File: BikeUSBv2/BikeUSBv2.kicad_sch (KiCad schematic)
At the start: 51 parts, among them J1 TYPE-C-31-M-16, J2 Conn_01x02_Female, Q1 SSM3J332R,LF, Q2 SSM3J332R,LF, SW1 SW_Push, SW2 SW_Push, U1 TPS63020DSJR, U2 ATtiny1616-M

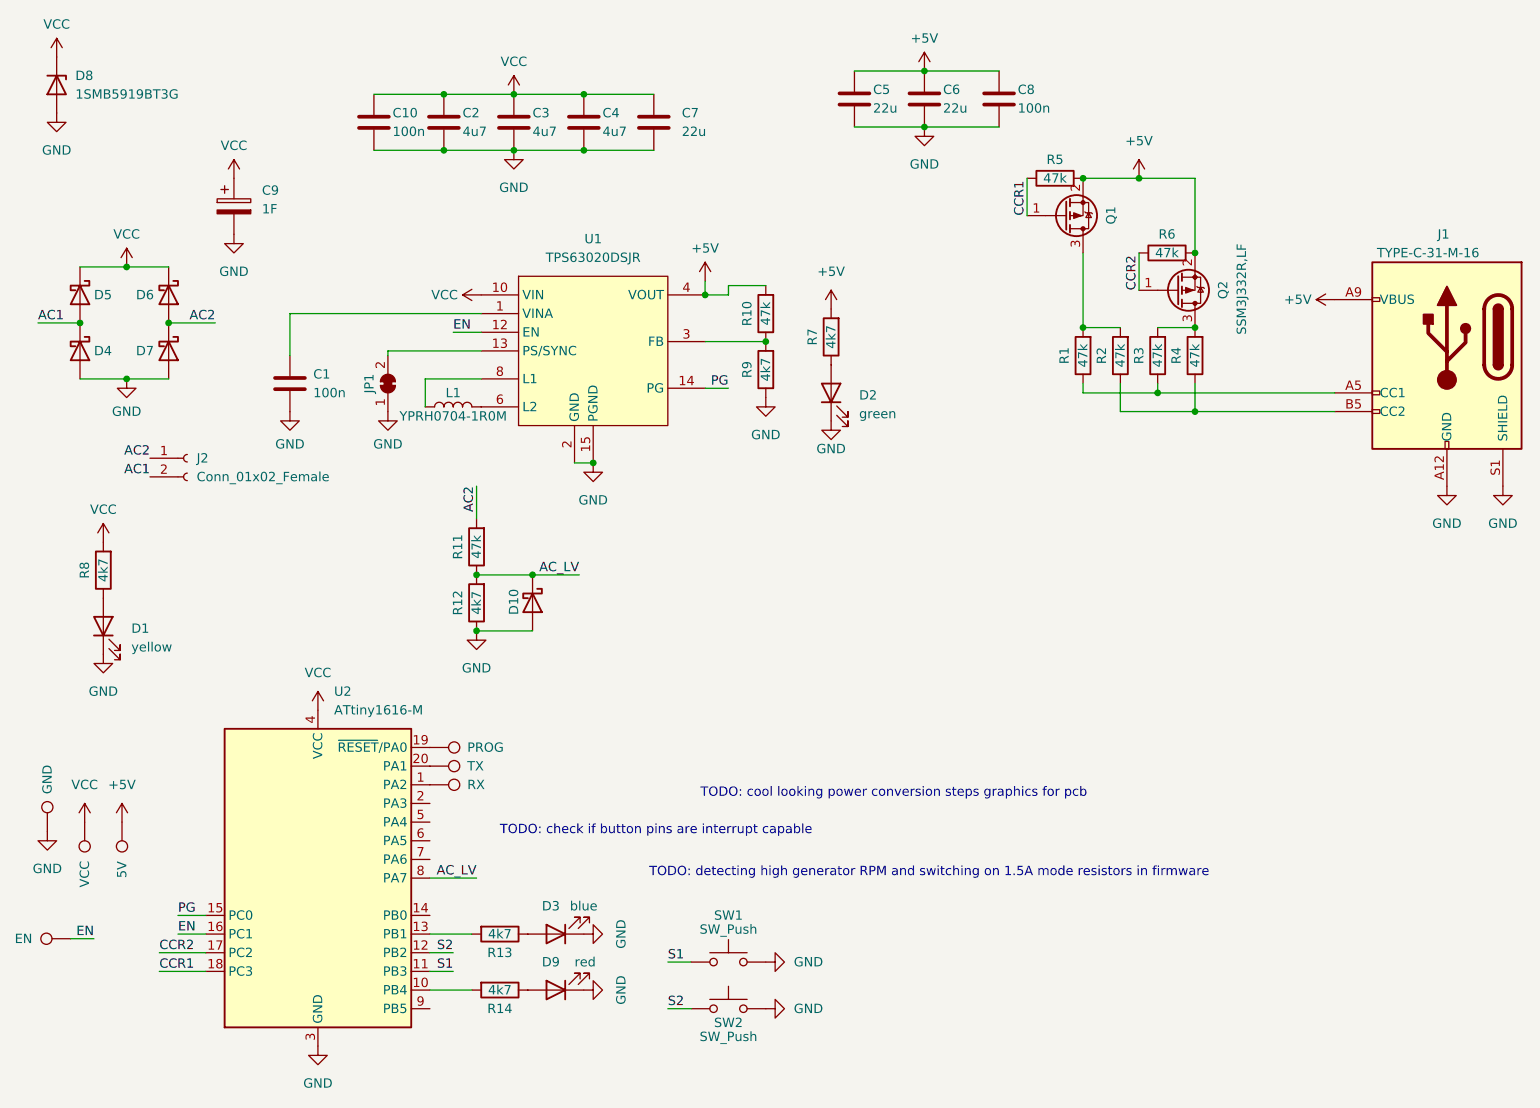
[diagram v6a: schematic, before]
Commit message: reduced component count
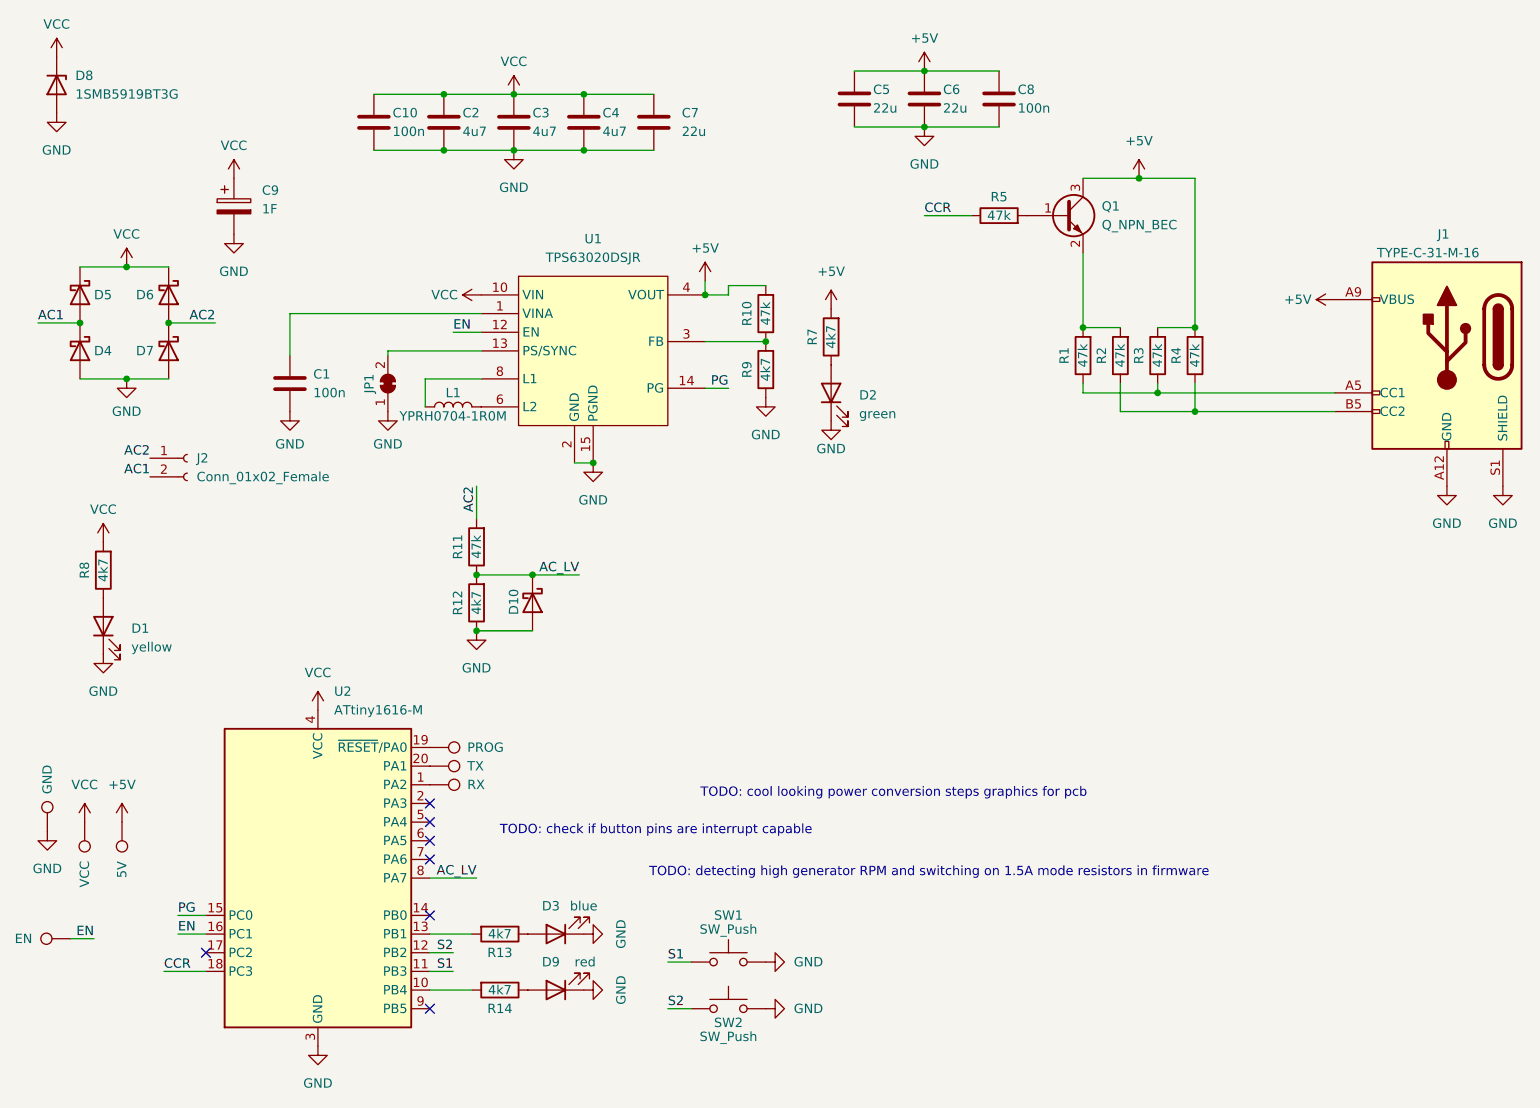
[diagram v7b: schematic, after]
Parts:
- removed Q1, Q2: SSM3J332R,LF, Package_TO_SOT_SMD:SOT-23_Handsoldering, symbol Device:Q_PMOS_GSD
- removed R6: 47k, Resistor_SMD:R_0805_2012Metric_Pad1.20x1.40mm_HandSolder, symbol Device:R
- added Q1: Q_NPN_BEC, Package_TO_SOT_SMD:SOT-23_Handsoldering, symbol Device:Q_NPN_BEC
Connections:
- net +5V: now also R3.2, R4.2, Q1.3 (C); no longer R5.2
- net at R1.2, R2.2: now also Q1.2 (E)
- net CCR1 renamed CCR
- net CCR2: no longer names the net of U2.17 (PC2)
- new net: Q1.1 (B), R5.2
- no-connect marks 0 -> 7
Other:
- moved on the sheet: R5
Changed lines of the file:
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@@
   (junction (at 85.09 122.555) (diameter 0) (color 0 0 0 0)
   )
-  (junction (at 160.02 68.58) (diameter 0) (color 0 0 0 0)
-  )
   (junction (at 29.845 80.645) (diameter 0) (color 0 0 0 0)
   )
@@
   (junction (at 92.075 64.77) (diameter 0) (color 0 0 0 0)
   )
+  (junction (at 175.26 88.9) (diameter 0) (color 0 0 0 0)
+  )
   (junction (at 93.345 107.315) (diameter 0) (color 0 0 0 0)
   )
@@
   (junction (at 138.43 53.975) (diameter 0) (color 0 0 0 0)
   )
-  (junction (at 175.26 88.9) (diameter 0) (color 0 0 0 0)
-  )
   (junction (at 77.47 122.555) (diameter 0) (color 0 0 0 0)
   )
@@
   (junction (at 167.64 68.58) (diameter 0) (color 0 0 0 0)
   )
-  (junction (at 175.26 78.74) (diameter 0) (color 0 0 0 0)
-  )
   (junction (at 175.26 100.33) (diameter 0) (color 0 0 0 0)
   )
+  (no_connect (at 71.12 153.67))
+  (no_connect (at 71.12 161.29))
+  (no_connect (at 71.12 168.91))
+  (no_connect (at 71.12 181.61))
+  (no_connect (at 71.12 156.21))
+  (no_connect (at 71.12 158.75))
+  (no_connect (at 40.64 173.99))
   (wire (pts (xy 165.1 100.33) (xy 165.1 96.52))
     (stroke (width 0) (type default))
@@
     (stroke (width 0) (type default))
   )
+  (wire (pts (xy 138.43 73.66) (xy 144.78 73.66))
+    (stroke (width 0) (type default))
+  )
   (wire (pts (xy 23.495 95.885) (xy 29.845 95.885))
     (stroke (width 0) (type default))
@@
     (stroke (width 0) (type default))
   )
-  (wire (pts (xy 167.64 78.74) (xy 167.64 83.82))
-    (stroke (width 0) (type default))
-  )
   (wire (pts (xy 170.18 97.79) (xy 170.18 96.52))
     (stroke (width 0) (type default))
@@
     (stroke (width 0) (type default))
   )
-  (wire (pts (xy 152.4 68.58) (xy 152.4 73.66))
-    (stroke (width 0) (type default))
-  )
   (wire (pts (xy 73.025 64.77) (xy 82.55 64.77))
     (stroke (width 0) (type default))
@@
     (stroke (width 0) (type default))
   )
+  (wire (pts (xy 175.26 68.58) (xy 175.26 88.9))
+    (stroke (width 0) (type default))
+  )
   (wire (pts (xy 82.55 57.15) (xy 92.075 57.15))
     (stroke (width 0) (type default))
@@
     (stroke (width 0) (type default))
   )
-  (wire (pts (xy 175.26 78.74) (xy 175.26 68.58))
-    (stroke (width 0) (type default))
-  )
   (wire (pts (xy 108.585 90.805) (xy 116.84 90.805))
     (stroke (width 0) (type default))
@@
     (stroke (width 0) (type default))
   )
-  (wire (pts (xy 34.29 173.99) (xy 40.64 173.99))
-    (stroke (width 0) (type default))
-  )
   (wire (pts (xy 128.905 53.975) (xy 138.43 53.975))
     (stroke (width 0) (type default))
@@
     (stroke (width 0) (type default))
   )
-  (wire (pts (xy 34.29 176.53) (xy 40.64 176.53))
+  (wire (pts (xy 34.925 176.53) (xy 40.64 176.53))
     (stroke (width 0) (type default))
   )
@@
     (effects (font (size 1.27 1.27)) (justify left bottom))
   )
-  (label "CCR2" (at 167.64 83.82 90) (fields_autoplaced)
-    (effects (font (size 1.27 1.27)) (justify left bottom))
-  )
   (label "S2" (at 74.295 173.99 180) (fields_autoplaced)
     (effects (font (size 1.27 1.27)) (justify right bottom))
   )
-  (label "CCR2" (at 34.29 173.99 0) (fields_autoplaced)
-    (effects (font (size 1.27 1.27)) (justify left bottom))
-  )
   (label "EN" (at 74.295 89.535 0) (fields_autoplaced)
     (effects (font (size 1.27 1.27)) (justify left bottom))
@@
     (effects (font (size 1.27 1.27)) (justify left bottom))
   )
-  (label "CCR1" (at 152.4 73.66 90) (fields_autoplaced)
+  (label "CCR" (at 138.43 73.66 0) (fields_autoplaced)
     (effects (font (size 1.27 1.27)) (justify left bottom))
   )
@@
     (effects (font (size 1.27 1.27)) (justify left bottom))
   )
-  (label "CCR1" (at 34.29 176.53 0) (fields_autoplaced)
+  (label "CCR" (at 34.925 176.53 0) (fields_autoplaced)
     (effects (font (size 1.27 1.27)) (justify left bottom))
   )
@@
     (effects (font (size 1.27 1.27)) (justify right bottom))
   )
-  (symbol (lib_id "Device:R") (at 156.21 68.58 90) (unit 1)
-    (in_bom yes) (on_board yes) (dnp no)
-    (property "Reference" "R5" (at 156.21 66.04 90)
-      (effects (font (size 1.27 1.27)))
-    )
-    (property "Value" "47k" (at 156.21 68.58 90)
-      (effects (font (size 1.27 1.27)))
-    )
-    (property "Footprint" "Resistor_SMD:R_0805_2012Metric_Pad1.20x1.40mm_HandSolder" (at 156.21 70.358 90)
-      (effects (font (size 1.27 1.27)) hide)
-    )
-    (property "Datasheet" "~" (at 156.21 68.58 0)
+  (symbol (lib_id "Device:R") (at 148.59 73.66 90) (unit 1)
+    (in_bom yes) (on_board yes) (dnp no)
+    (property "Reference" "R5" (at 148.59 71.12 90)
+      (effects (font (size 1.27 1.27)))
+    )
+    (property "Value" "47k" (at 148.59 73.66 90)
+      (effects (font (size 1.27 1.27)))
+    )
+    (property "Footprint" "Resistor_SMD:R_0805_2012Metric_Pad1.20x1.40mm_HandSolder" (at 148.59 75.438 90)
+      (effects (font (size 1.27 1.27)) hide)
+    )
+    (property "Datasheet" "~" (at 148.59 73.66 0)
       (effects (font (size 1.27 1.27)) hide)
     )
@@
     )
   )
+  (symbol (lib_id "Device:Q_NPN_BEC") (at 157.48 73.66 0) (unit 1)
+    (in_bom yes) (on_board yes) (dnp no) (fields_autoplaced)
+    (property "Reference" "Q1" (at 162.56 72.39 0)
+      (effects (font (size 1.27 1.27)) (justify left))
+    )
+    (property "Value" "Q_NPN_BEC" (at 162.56 74.93 0)
+      (effects (font (size 1.27 1.27)) (justify left))
+    )
+    (property "Footprint" "Package_TO_SOT_SMD:SOT-23_Handsoldering" (at 162.56 71.12 0)
+      (effects (font (size 1.27 1.27)) hide)
+    )
+    (property "Datasheet" "~" (at 157.48 73.66 0)
+      (effects (font (size 1.27 1.27)) hide)
+    )
+    (pin "1")
+    (pin "3")
+    (pin "2")
+    (instances
+      (project "BikeUSBv2"
+        (path "/b4aff538-5116-4944-9d24-c26a88d7dfe8"
+          (reference "Q1") (unit 1)
+        )
+      )
+    )
+  )
   (symbol (lib_id "power:GND") (at 93.345 107.315 0) (mirror y) (unit 1)
     (in_bom yes) (on_board yes) (dnp no) (fields_autoplaced)
@@
         (path "/b4aff538-5116-4944-9d24-c26a88d7dfe8"
           (reference "#PWR033") (unit 1)
-        )
-      )
-    )
-  )
-  (symbol (lib_id "Device:Q_PMOS_GSD") (at 172.72 83.82 0) (mirror x) (unit 1)
-    (in_bom yes) (on_board yes) (dnp no)
-    (property "Reference" "Q2" (at 179.07 82.55 90)
-      (effects (font (size 1.27 1.27)) (justify left))
-    )
-    (property "Value" "SSM3J332R,LF" (at 181.61 77.47 90)
-      (effects (font (size 1.27 1.27)) (justify left))
-    )
-    (property "Footprint" "Package_TO_SOT_SMD:SOT-23_Handsoldering" (at 177.8 86.36 0)
-      (effects (font (size 1.27 1.27)) hide)
-    )
-    (property "Datasheet" "~" (at 172.72 83.82 0)
-      (effects (font (size 1.27 1.27)) hide)
-    )
-    (pin "2")
-    (pin "1")
-    (pin "3")
-    (instances
-      (project "BikeUSBv2"
-        (path "/b4aff538-5116-4944-9d24-c26a88d7dfe8"
-          (reference "Q2") (unit 1)
         )
       )
@@
     )
   )
-  (symbol (lib_id "Device:Q_PMOS_GSD") (at 157.48 73.66 0) (mirror x) (unit 1)
-    (in_bom yes) (on_board yes) (dnp no)
-    (property "Reference" "Q1" (at 163.83 72.39 90)
-      (effects (font (size 1.27 1.27)) (justify left))
-    )
-    (property "Value" "SSM3J332R,LF" (at 157.48 74.93 90)
-      (effects (font (size 1.27 1.27)) (justify left) hide)
-    )
-    (property "Footprint" "Package_TO_SOT_SMD:SOT-23_Handsoldering" (at 162.56 76.2 0)
-      (effects (font (size 1.27 1.27)) hide)
-    )
-    (property "Datasheet" "~" (at 157.48 73.66 0)
-      (effects (font (size 1.27 1.27)) hide)
-    )
-    (pin "2")
-    (pin "1")
-    (pin "3")
-    (instances
-      (project "BikeUSBv2"
-        (path "/b4aff538-5116-4944-9d24-c26a88d7dfe8"
-          (reference "Q1") (unit 1)
-        )
-      )
-    )
-  )
   (symbol (lib_id "Device:C") (at 73.025 60.96 0) (unit 1)
     (in_bom yes) (on_board yes) (dnp no)
@@
         )
       )
-    )
-  )
-  (symbol (lib_id "Device:R") (at 171.45 78.74 90) (unit 1)
-    (in_bom yes) (on_board yes) (dnp no)
-    (property "Reference" "R6" (at 171.45 76.2 90)
-      (effects (font (size 1.27 1.27)))
-    )
-    (property "Value" "47k" (at 171.45 78.74 90)
-      (effects (font (size 1.27 1.27)))
-    )
-    (property "Footprint" "Resistor_SMD:R_0805_2012Metric_Pad1.20x1.40mm_HandSolder" (at 171.45 80.518 90)
-      (effects (font (size 1.27 1.27)) hide)
-    )
-    (property "Datasheet" "~" (at 171.45 78.74 0)
-      (effects (font (size 1.27 1.27)) hide)
-    )
-    (pin "1")
-    (pin "2")
-    (instances
-      (project "BikeUSBv2"
-        (path "/b4aff538-5116-4944-9d24-c26a88d7dfe8"
-          (reference "R6") (unit 1)
-        )
-      )

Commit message: better layout
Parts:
- added C11: 100n, Capacitor_SMD:C_0805_2012Metric_Pad1.18x1.45mm_HandSolder, symbol Device:C
- renumbered R3 to R1, R4 to R2, R1 to R3, R2 to R4
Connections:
- net +5V: now also C11.1
- net GND: now also C11.2
